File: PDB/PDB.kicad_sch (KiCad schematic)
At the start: 22 parts, among them U2 STM32H742VGTx

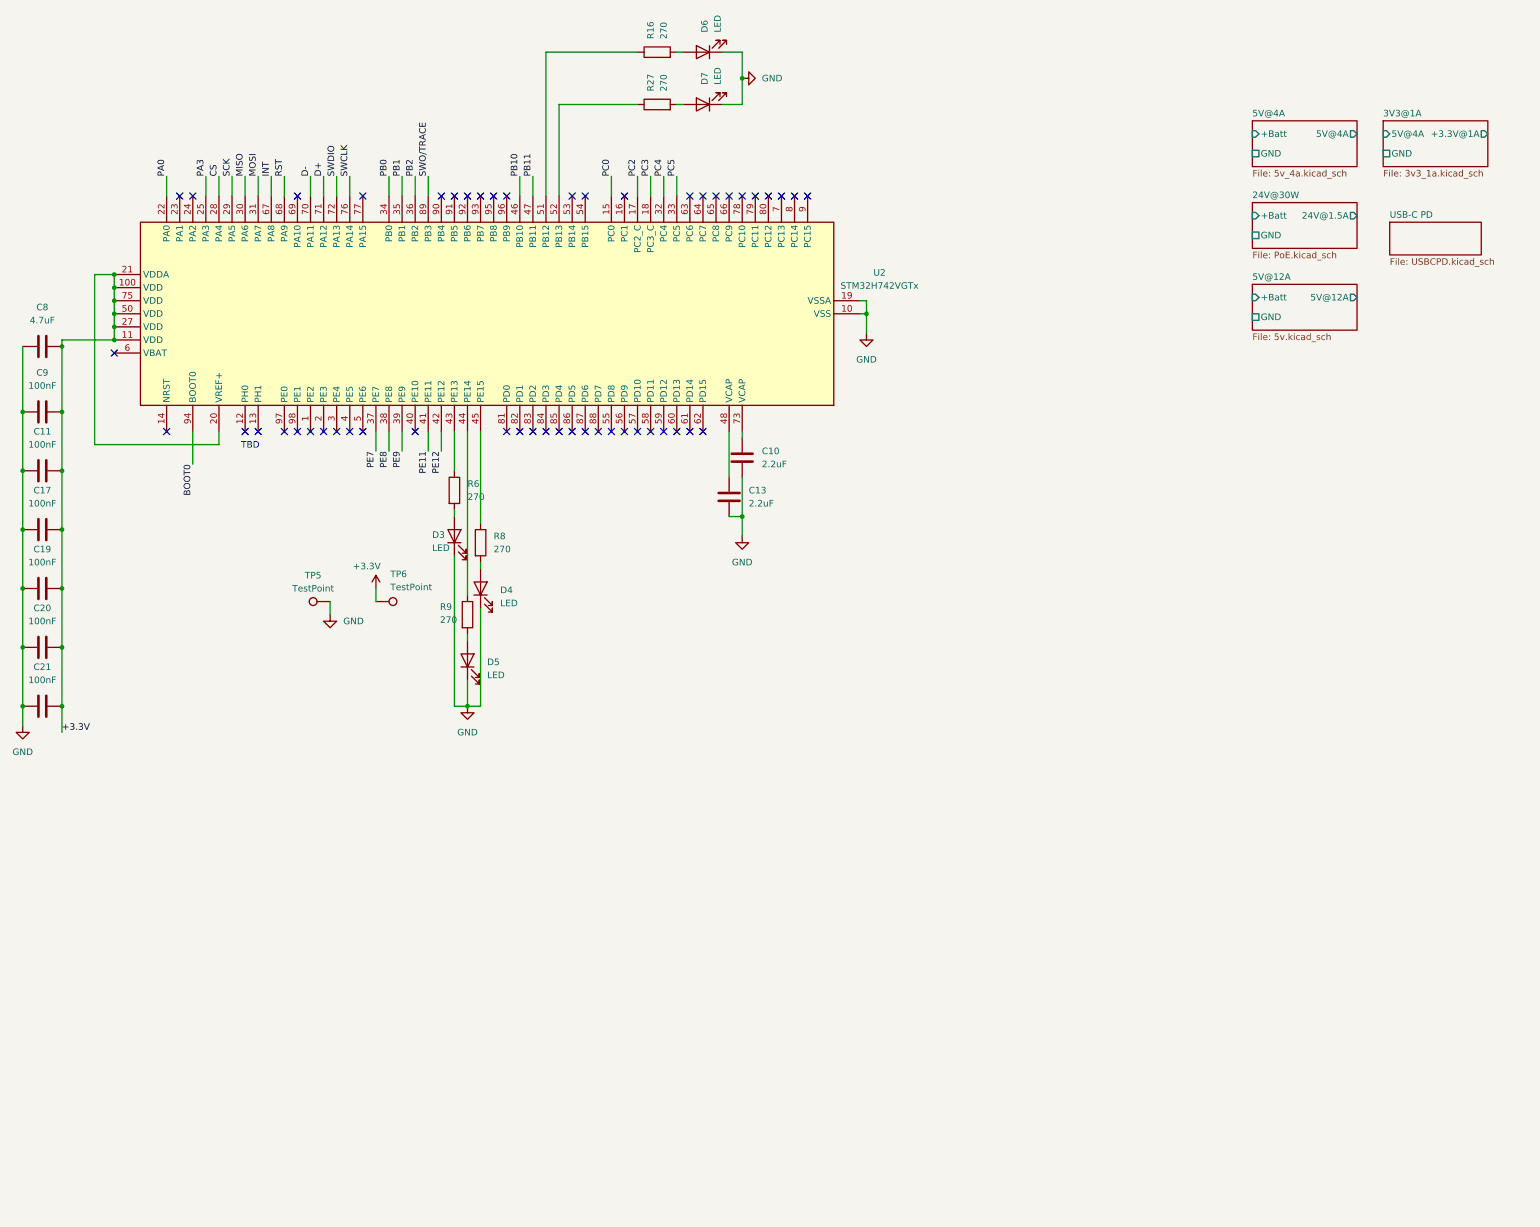
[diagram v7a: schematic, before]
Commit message: added sd card
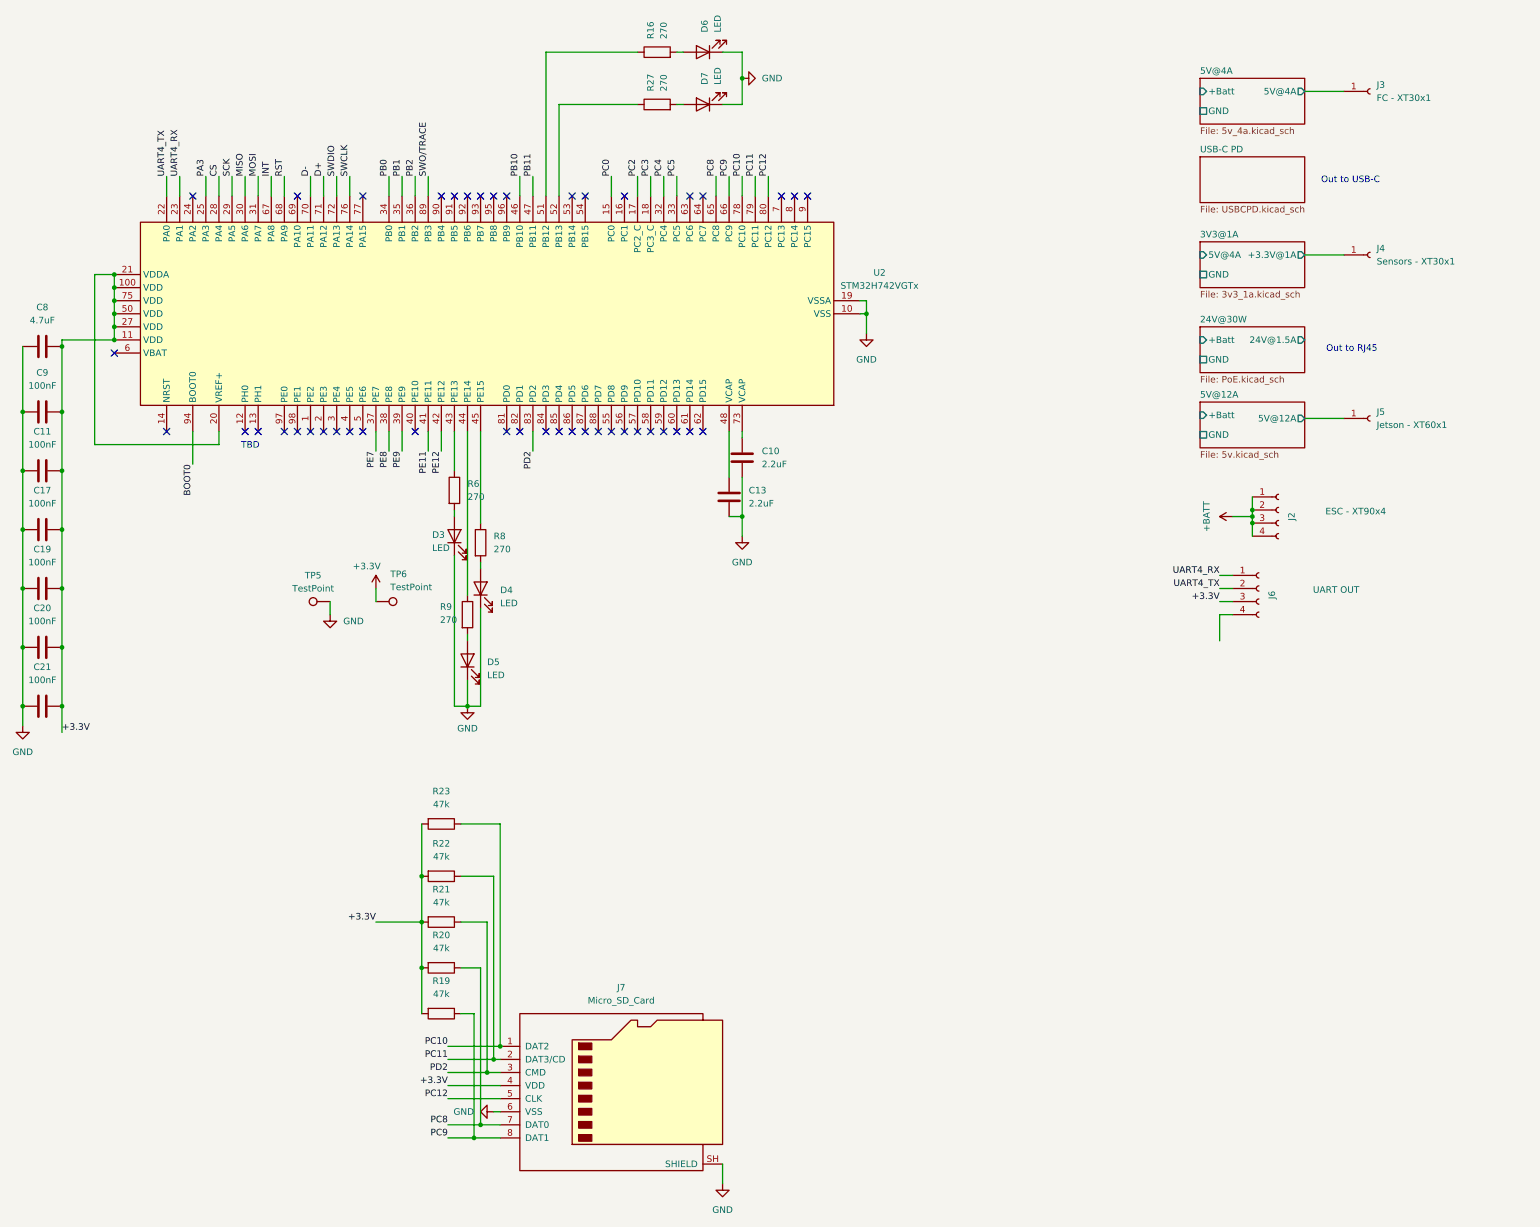
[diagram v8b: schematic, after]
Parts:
- added J2: ESC - XT90x4, symbol Connector:Conn_01x04_Socket
- added J3: FC - XT30x1, symbol Connector:Conn_01x01_Socket
- added J4: Sensors - XT30x1, symbol Connector:Conn_01x01_Socket
- added J5: Jetson - XT60x1, symbol Connector:Conn_01x01_Socket
- added J6: UART OUT, symbol Connector:Conn_01x04_Socket
- added J7: Micro_SD_Card, symbol Connector:Micro_SD_Card
- added R19, R20, R21, R22, R23: 47k, Resistor_SMD:R_0603_1608Metric_Pad0.98x0.95mm_HandSolder, symbol Device:R
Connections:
- net +3.3V: now also J6.3 (Pin_3), J7.4 (VDD), R19.2, R20.2, R21.2, R22.2, R23.2
- net 3V3@1A/+3.3V@1A: now also J4.1 (Pin_1)
- net 5V@12A/5V@12A: now also J5.1 (Pin_1)
- net 5V@4A/5V@4A: now also J3.1 (Pin_1)
- net GND: now also J7.6 (VSS), J7.SH (SHIELD)
- net UART4_RX: now reaches U2.23 (PA1)
- net UART4_RX: now also J6.1 (Pin_1)
- net PC8: now reaches U2.65 (PC8)
- net PC8: now also J7.7 (DAT0), R20.1
- net PC9: now reaches U2.66 (PC9)
- net PC9: now also J7.8 (DAT1), R19.1
- net PC10: now reaches U2.78 (PC10)
- net PC10: now also J7.1 (DAT2), R23.1
- net PC11: now reaches U2.79 (PC11)
- net PC11: now also J7.2 (DAT3/CD), R22.1
- net PC12: now reaches U2.80 (PC12)
- net PC12: now also J7.5 (CLK)
- net PD2: now reaches U2.83 (PD2)
- net PD2: now also J7.3 (CMD), R21.1
- net PA0 renamed UART4_TX
- net UART4_TX: now also J6.2 (Pin_2)
- new net +BATT: J2.1 (Pin_1), J2.2 (Pin_2), J2.3 (Pin_3), J2.4 (Pin_4)
- no-connect marks 51 -> 44
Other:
- note added: "Out to RJ45"
- note added: "Out to USB-C"
